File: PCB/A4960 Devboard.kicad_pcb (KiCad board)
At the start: 2 copper layers, 56 parts, among them IC1 ATMEGA8-AI, P1 CONN_02X03, P2 CONN_01X02, P3 CONN_01X03, P4 CONN_01X03, Q1 Q_NMOS_GDS_old, Q2 Q_NMOS_GDS_old, Q3 Q_NMOS_GDS_old, Q4 Q_NMOS_GDS_old, Q5 Q_NMOS_GDS_old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

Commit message: PCB weiter
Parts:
- moved Q6 39.8 mm to (232.2, 85.5)
- moved Q5 39.4 mm to (232.2, 77.5)
- moved U2 30.7 mm to (228.3, 99.8)
- moved U1 27.9 mm to (175.4, 86.7)
- moved Q3 27.3 mm to (223.0, 77.5), turned to 0 degrees
- moved P4 26.4 mm to (221.0, 68.3), turned to 90 degrees
- moved P2 16.4 mm to (206.2, 68.6), turned to 270 degrees
- moved Q4 12.9 mm to (223.0, 85.6), turned to 0 degrees
- moved IC1 12.7 mm to (204.0, 99.8)
- moved C21 5.80 mm to (189.6, 74.7)
- moved Q1 0.25 mm to (213.9, 77.5)
- moved Q2 0.25 mm to (213.9, 85.6)

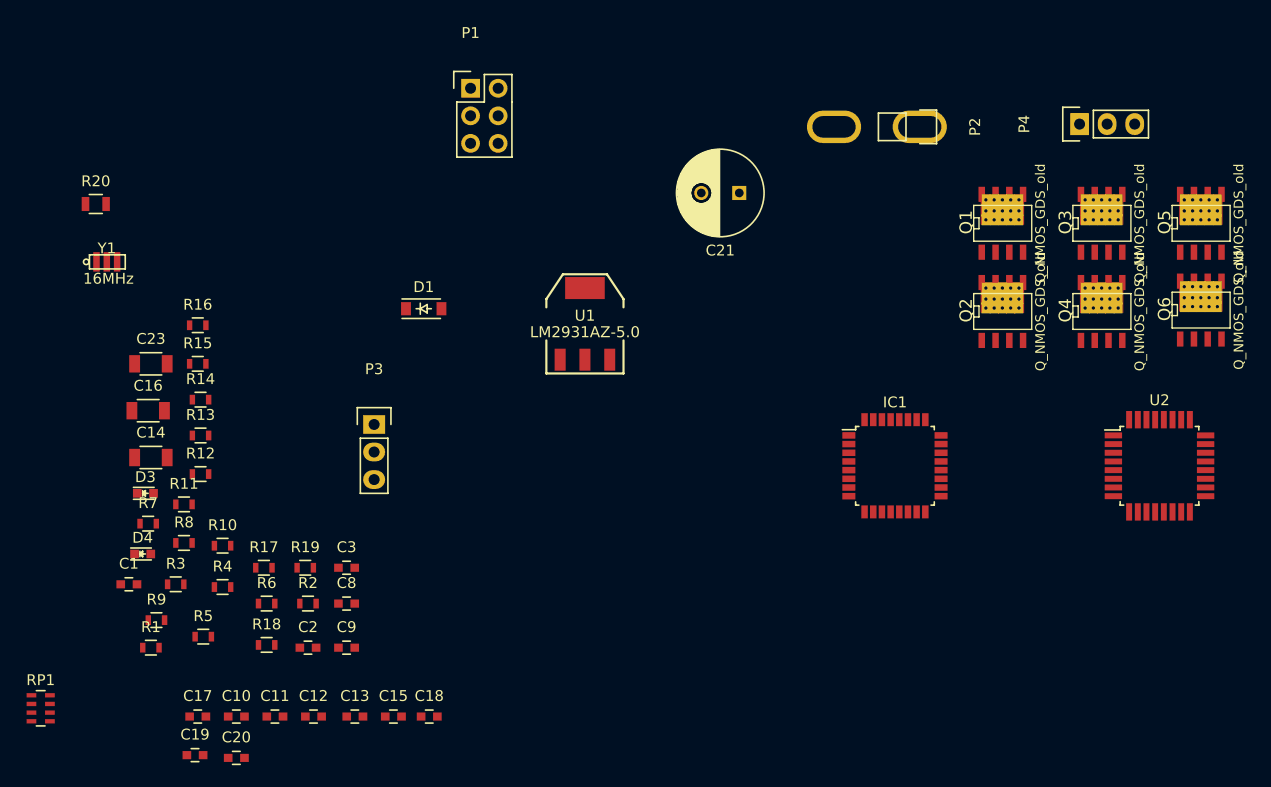
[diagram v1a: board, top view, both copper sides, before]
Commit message: PCB weiter gemcht & neuer Spannungswandler auf 5V
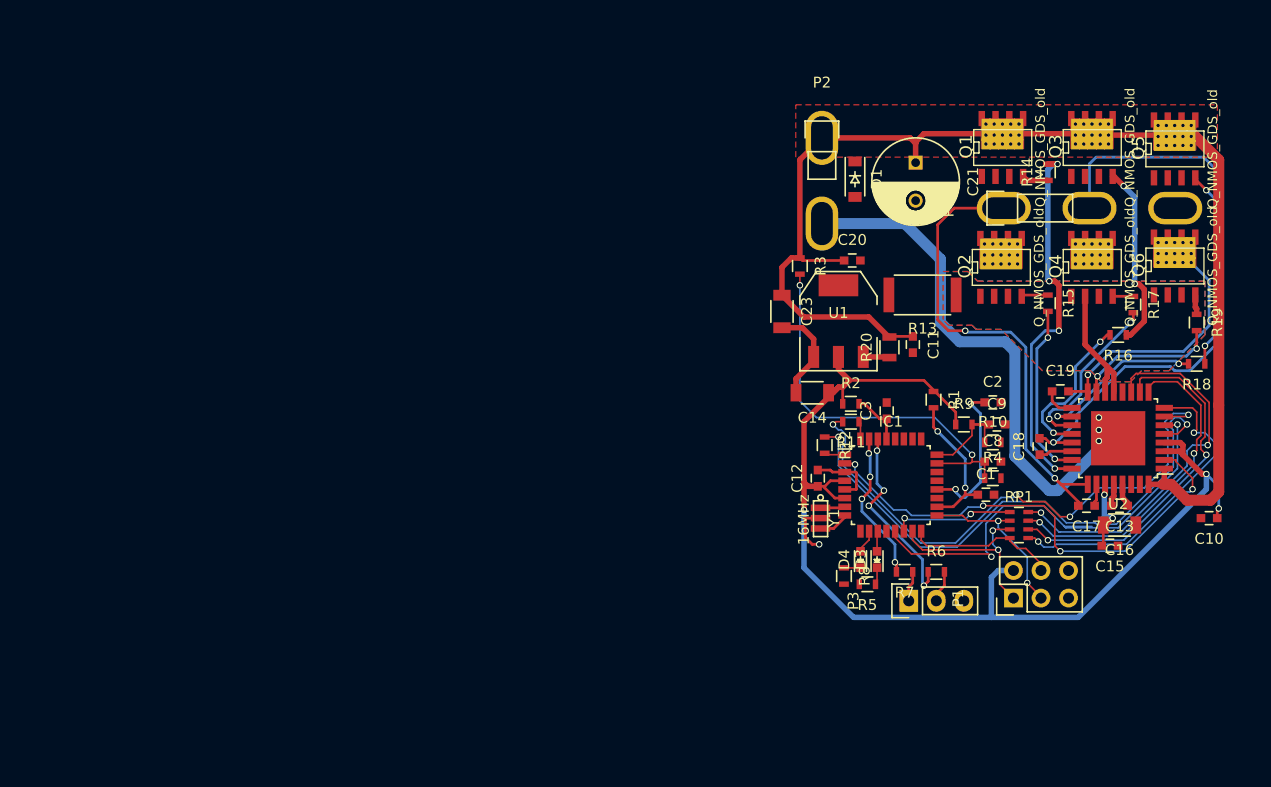
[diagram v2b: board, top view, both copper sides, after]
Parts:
- R13: footprint Resistors_SMD:R_0603 -> Resistors_SMD:R_2512
- U1: value LM2931AZ-5.0 -> LD1117S50TR; footprint toni:SOT223_GND_VO_VI -> TO_SOT_Packages_SMD:SOT-223
- moved RP1 91.7 mm to (215.4, 105.3)
- moved C10 91.5 mm to (232.9, 104.6), turned to 180 degrees
- moved C16 90.2 mm to (224.7, 105.3), turned to 180 degrees
- moved R18 89.6 mm to (231.8, 90.4), turned to 180 degrees
- moved C19 86.5 mm to (219.2, 93.0)
- moved R19 85.2 mm to (231.8, 86.6), turned to 270 degrees
- moved R16 84.8 mm to (224.5, 87.8), turned to 180 degrees
- moved C17 84.2 mm to (221.6, 103.5), turned to 180 degrees
- moved R17 83.7 mm to (225.9, 85.0), turned to 270 degrees
- moved R14 80.9 mm to (218.1, 72.8), turned to 90 degrees
- moved C1 79.4 mm to (212.3, 102.5)
- moved R15 78.6 mm to (218.1, 84.8), turned to 270 degrees
- moved R9 76.6 mm to (210.3, 96.0)
- moved R1 75.7 mm to (207.5, 93.7), turned to 270 degrees
- moved R20 74.3 mm to (203.5, 88.9), turned to 90 degrees
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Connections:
- C10 pad 1: Net-(C10-Pad1) -> +3V3
- U2 pad 3: Net-(C10-Pad1) -> +3V3
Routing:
- net VPP: track 0.00 -> 125.7 mm
- net +3V3: track 0.00 -> 109.8 mm, vias 0 -> 3
- net GND: track 0.00 -> 76.0 mm, vias 0 -> 4
- net /MotorB: track 0.00 -> 55.5 mm, vias 0 -> 1
- net Net-(R11-Pad2): track 0.00 -> 52.0 mm, vias 0 -> 4
- net Net-(R12-Pad1): track 0.00 -> 51.4 mm, vias 0 -> 2
- net Net-(R14-Pad2): track 0.00 -> 47.8 mm, vias 0 -> 4
- net Net-(IC1-Pad2): track 0.00 -> 44.9 mm, vias 0 -> 4
- net /MotorA: track 0.00 -> 44.6 mm, vias 0 -> 2
- net Net-(IC1-Pad13): track 0.00 -> 42.7 mm, vias 0 -> 2
- net /ADC0: track 0.00 -> 36.2 mm, vias 0 -> 2
- net Net-(RP1-Pad8): track 0.00 -> 35.2 mm, vias 0 -> 2
- net Net-(RP1-Pad6): track 0.00 -> 33.6 mm, vias 0 -> 2
- net Net-(Q3-PadG): track 0.00 -> 32.5 mm, vias 0 -> 2
- net Net-(RP1-Pad7): track 0.00 -> 30.7 mm, vias 0 -> 2
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- added copper zone on B.Cu, net /LSS
- added copper zone on F.Cu, net /LSS
- added copper zone on F.Cu, net VPP
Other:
- net class Default: clearance 0.2 -> 0.1778; trace_width 0.25 -> 0.1524
- rule trace_clearance: 0.2 -> 0.1778
- rule trace_min: 0.2 -> 0.1524

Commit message: PCB fertig!
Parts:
- Q1, Q2, Q3, Q4, Q5, Q6: footprint sven:SO8_WITH_Heatpipes -> Sven:SO8_WITH_Heatpipes_New
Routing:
- net GND: track 76.0 -> 121.4 mm, vias 4 -> 11
- net /Reset: track 4.99 -> 34.7 mm, vias 0 -> 4
- net /MotorB: track 55.5 -> 66.0 mm
- net /MotorC: track 23.0 -> 33.0 mm
- net /MotorA: track 44.6 -> 51.8 mm
- net VPP: track 125.7 -> 126.7 mm
- net +3V3: track 109.8 -> 110.6 mm
- net /SCK: track 15.7 -> 15.8 mm, vias 2 -> 1
- added copper zone on F.Cu, net /MotorA
- added copper zone on F.Cu, net /MotorB
- added copper zone on F.Cu, net /MotorC
- added copper zone on B.Cu, net GND
- added copper zone on F.Cu, net GND
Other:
- board outline added: 43.4 x 48.8 mm

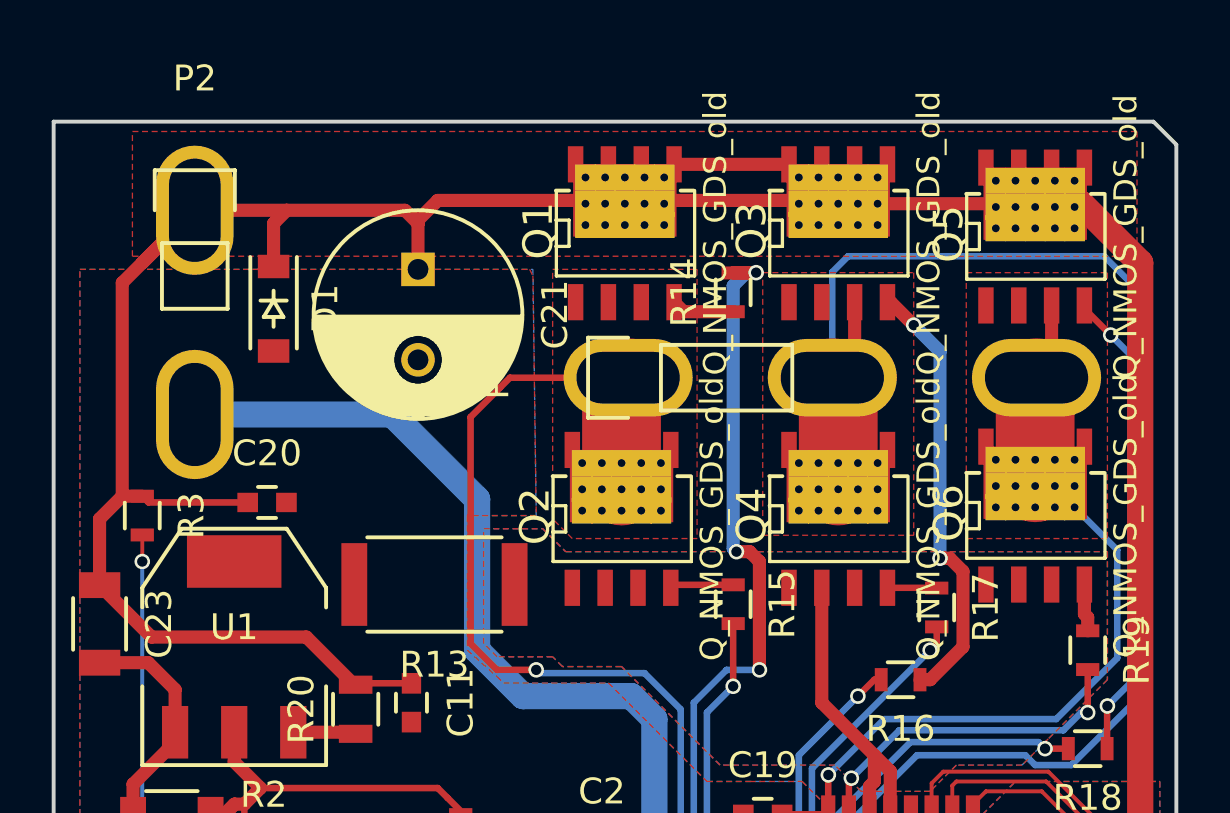
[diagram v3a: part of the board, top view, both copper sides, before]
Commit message: Vcc-Fläche oben eingefügt.
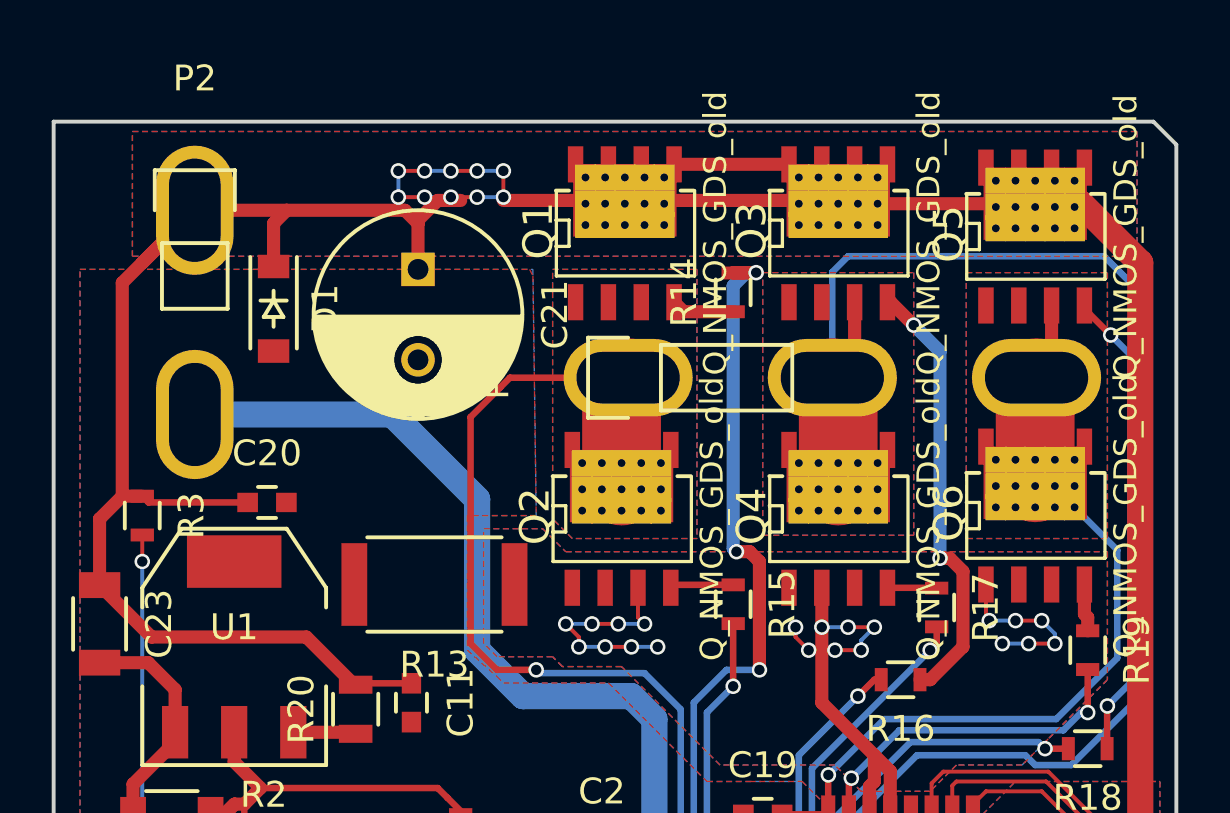
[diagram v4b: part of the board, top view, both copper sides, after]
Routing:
- net /LSS: track 12.4 -> 35.5 mm, vias 0 -> 21
- net VPP: track 126.7 -> 136.0 mm, vias 0 -> 10
- added copper zone on B.Cu, net /MotorA
- added copper zone on B.Cu, net /MotorB
- added copper zone on B.Cu, net /MotorC
- added copper zone on B.Cu, net VPP
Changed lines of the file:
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@@
     (links 256)
     (no_connects 0)
-    (area 0 0 0 0)
+    (area 190.1452 63.3932 235.279001 117.354133)
     (thickness 1.6)
     (drawings 8)
-    (tracks 716)
+    (tracks 790)
     (zones 0)
     (modules 56)
@@
   )
   (setup
-    (last_trace_width 0.508)
+    (last_trace_width 0.1524)
     (user_trace_width 0.1524)
     (user_trace_width 0.254)
@@
   (segment (start 212.229 96.012) (end 212.229 97.663) (width 0.1524) (layer F.Cu) (net 6))
   (segment (start 211.062 96.012) (end 212.229 96.012) (width 0.1524) (layer F.Cu) (net 6))
+  (via (at 209.169 69.088) (size 0.6) (drill 0.4) (layers F.Cu B.Cu) (net 7))
+  (segment (start 207.137 69.088) (end 208.153 69.088) (width 0.1524) (layer F.Cu) (net 7))
+  (via (at 208.153 69.088) (size 0.6) (drill 0.4) (layers F.Cu B.Cu) (net 7))
+  (segment (start 208.153 69.088) (end 209.169 69.088) (width 0.1524) (layer B.Cu) (net 7))
+  (segment (start 209.169 69.215) (end 209.169 69.088) (width 0.1524) (layer F.Cu) (net 7))
+  (segment (start 209.169 69.088) (end 209.169 68.072) (width 0.1524) (layer F.Cu) (net 7))
+  (segment (start 207.518 69.088) (end 207.518 69.215) (width 0.1524) (layer F.Cu) (net 7))
+  (segment (start 207.391 69.215) (end 207.518 69.088) (width 0.1524) (layer F.Cu) (net 7))
+  (segment (start 207.264 69.215) (end 207.391 69.215) (width 0.1524) (layer F.Cu) (net 7))
+  (segment (start 207.137 69.088) (end 207.264 69.215) (width 0.1524) (layer F.Cu) (net 7))
+  (via (at 207.137 69.088) (size 0.6) (drill 0.4) (layers F.Cu B.Cu) (net 7))
+  (segment (start 206.121 69.088) (end 207.137 69.088) (width 0.1524) (layer B.Cu) (net 7))
+  (via (at 206.121 69.088) (size 0.6) (drill 0.4) (layers F.Cu B.Cu) (net 7))
+  (segment (start 205.105 69.088) (end 206.121 69.088) (width 0.1524) (layer F.Cu) (net 7))
+  (via (at 205.105 69.088) (size 0.6) (drill 0.4) (layers F.Cu B.Cu) (net 7))
+  (segment (start 205.105 68.072) (end 205.105 69.088) (width 0.1524) (layer B.Cu) (net 7))
+  (via (at 205.105 68.072) (size 0.6) (drill 0.4) (layers F.Cu B.Cu) (net 7))
+  (segment (start 206.121 68.072) (end 205.105 68.072) (width 0.1524) (layer F.Cu) (net 7))
+  (via (at 206.121 68.072) (size 0.6) (drill 0.4) (layers F.Cu B.Cu) (net 7))
+  (segment (start 207.137 68.072) (end 206.121 68.072) (width 0.1524) (layer B.Cu) (net 7))
+  (via (at 207.137 68.072) (size 0.6) (drill 0.4) (layers F.Cu B.Cu) (net 7))
+  (segment (start 208.153 68.072) (end 207.137 68.072) (width 0.1524) (layer F.Cu) (net 7))
+  (via (at 208.153 68.072) (size 0.6) (drill 0.4) (layers F.Cu B.Cu) (net 7))
+  (segment (start 209.169 68.072) (end 208.153 68.072) (width 0.1524) (layer B.Cu) (net 7))
+  (via (at 209.169 68.072) (size 0.6) (drill 0.4) (layers F.Cu B.Cu) (net 7))
   (segment (start 194.425 80.657) (end 194.425 72.402) (width 0.508) (layer F.Cu) (net 7))
   (segment (start 194.425 72.402) (end 197.231 69.596) (width 0.508) (layer F.Cu) (net 7))
@@
   (segment (start 228.668 101.532) (end 228.786 101.414) (width 0.508) (layer F.Cu) (net 7))
   (segment (start 205.867 70.104) (end 205.867 69.977) (width 0.508) (layer F.Cu) (net 7))
-  (segment (start 206.629 69.215) (end 222.123 69.215) (width 0.508) (layer F.Cu) (net 7))
   (segment (start 205.867 69.977) (end 206.629 69.215) (width 0.508) (layer F.Cu) (net 7))
+  (segment (start 206.629 69.215) (end 207.518 69.215) (width 0.508) (layer F.Cu) (net 7))
+  (segment (start 209.169 69.215) (end 222.123 69.215) (width 0.508) (layer F.Cu) (net 7))
   (segment (start 222.123 69.215) (end 222.25 69.342) (width 0.508) (layer F.Cu) (net 7))
   (segment (start 222.25 69.342) (end 229.743 69.342) (width 0.508) (layer F.Cu) (net 7))
@@
   (segment (start 200.781 97.35) (end 200.781 95.891) (width 0.1524) (layer F.Cu) (net 41))
   (segment (start 200.781 95.891) (end 200.648 95.758) (width 0.1524) (layer F.Cu) (net 41))
+  (segment (start 214.376 84.201) (end 214.376 85.344) (width 0.1524) (layer F.Cu) (net 42) (status 400000))
+  (segment (start 214.376 85.344) (end 214.63 85.598) (width 0.1524) (layer F.Cu) (net 42))
+  (via (at 214.63 85.598) (size 0.6) (drill 0.4) (layers F.Cu B.Cu) (net 42))
+  (segment (start 214.63 85.598) (end 213.614 85.598) (width 0.1524) (layer B.Cu) (net 42))
+  (via (at 213.614 85.598) (size 0.6) (drill 0.4) (layers F.Cu B.Cu) (net 42))
+  (segment (start 213.614 85.598) (end 212.598 85.598) (width 0.1524) (layer F.Cu) (net 42))
+  (via (at 212.598 85.598) (size 0.6) (drill 0.4) (layers F.Cu B.Cu) (net 42))
+  (segment (start 212.598 85.598) (end 211.582 85.598) (width 0.1524) (layer B.Cu) (net 42))
+  (via (at 211.582 85.598) (size 0.6) (drill 0.4) (layers F.Cu B.Cu) (net 42))
+  (segment (start 211.582 85.598) (end 212.09 86.106) (width 0.1524) (layer F.Cu) (net 42))
+  (segment (start 212.09 86.106) (end 212.09 86.487) (width 0.1524) (layer F.Cu) (net 42))
+  (via (at 212.09 86.487) (size 0.6) (drill 0.4) (layers F.Cu B.Cu) (net 42))
+  (segment (start 212.09 86.487) (end 213.106 86.487) (width 0.1524) (layer B.Cu) (net 42))
+  (via (at 213.106 86.487) (size 0.6) (drill 0.4) (layers F.Cu B.Cu) (net 42))
+  (segment (start 213.106 86.487) (end 214.122 86.487) (width 0.1524) (layer F.Cu) (net 42))
+  (via (at 214.122 86.487) (size 0.6) (drill 0.4) (layers F.Cu B.Cu) (net 42))
+  (segment (start 214.122 86.487) (end 215.138 86.487) (width 0.1524) (layer B.Cu) (net 42))
+  (via (at 215.138 86.487) (size 0.6) (drill 0.4) (layers F.Cu B.Cu) (net 42))
+  (segment (start 227.838 84.074) (end 227.838 85.344) (width 0.1524) (layer F.Cu) (net 42) (status 400000))
+  (segment (start 227.838 85.344) (end 227.965 85.471) (width 0.1524) (layer F.Cu) (net 42))
+  (via (at 227.965 85.471) (size 0.6) (drill 0.4) (layers F.Cu B.Cu) (net 42))
+  (segment (start 227.965 85.471) (end 228.981 85.471) (width 0.1524) (layer B.Cu) (net 42))
+  (via (at 228.981 85.471) (size 0.6) (drill 0.4) (layers F.Cu B.Cu) (net 42))
+  (segment (start 228.981 85.471) (end 229.997 85.471) (width 0.1524) (layer F.Cu) (net 42))
+  (via (at 229.997 85.471) (size 0.6) (drill 0.4) (layers F.Cu B.Cu) (net 42))
+  (segment (start 229.997 85.471) (end 230.505 85.979) (width 0.1524) (layer B.Cu) (net 42))
+  (segment (start 230.505 85.979) (end 230.505 86.36) (width 0.1524) (layer B.Cu) (net 42))
+  (via (at 230.505 86.36) (size 0.6) (drill 0.4) (layers F.Cu B.Cu) (net 42))
+  (segment (start 230.505 86.36) (end 229.489 86.36) (width 0.1524) (layer F.Cu) (net 42))
+  (via (at 229.489 86.36) (size 0.6) (drill 0.4) (layers F.Cu B.Cu) (net 42))
+  (segment (start 229.489 86.36) (end 228.473 86.36) (width 0.1524) (layer B.Cu) (net 42))
+  (via (at 228.473 86.36) (size 0.6) (drill 0.4) (layers F.Cu B.Cu) (net 42))
+  (segment (start 221.488 84.201) (end 221.488 85.725) (width 0.1524) (layer F.Cu) (net 42) (status 400000))
+  (via (at 221.488 85.725) (size 0.6) (drill 0.4) (layers F.Cu B.Cu) (net 42))
+  (segment (start 221.488 85.725) (end 222.504 85.725) (width 0.1524) (layer B.Cu) (net 42))
+  (via (at 222.504 85.725) (size 0.6) (drill 0.4) (layers F.Cu B.Cu) (net 42))
+  (segment (start 222.504 85.725) (end 223.52 85.725) (width 0.1524) (layer F.Cu) (net 42))
+  (via (at 223.52 85.725) (size 0.6) (drill 0.4) (layers F.Cu B.Cu) (net 42))
+  (segment (start 223.52 85.725) (end 223.012 86.233) (width 0.1524) (layer B.Cu) (net 42))
+  (segment (start 223.012 86.233) (end 223.012 86.614) (width 0.1524) (layer B.Cu) (net 42))
+  (via (at 223.012 86.614) (size 0.6) (drill 0.4) (layers F.Cu B.Cu) (net 42))
+  (segment (start 223.012 86.614) (end 221.996 86.614) (width 0.1524) (layer F.Cu) (net 42))
+  (via (at 221.996 86.614) (size 0.6) (drill 0.4) (layers F.Cu B.Cu) (net 42))
+  (segment (start 221.996 86.614) (end 220.98 86.614) (width 0.1524) (layer B.Cu) (net 42))
+  (via (at 220.98 86.614) (size 0.6) (drill 0.4) (layers F.Cu B.Cu) (net 42))
+  (segment (start 220.98 86.614) (end 220.472 86.106) (width 0.1524) (layer F.Cu) (net 42))
+  (segment (start 220.472 86.106) (end 220.472 85.725) (width 0.1524) (layer F.Cu) (net 42))
+  (via (at 220.472 85.725) (size 0.6) (drill 0.4) (layers F.Cu B.Cu) (net 42))
   (segment (start 224.136 93.032) (end 224.136 91.294) (width 0.508) (layer F.Cu) (net 42))
   (segment (start 224.136 91.294) (end 223.52 90.678) (width 0.508) (layer F.Cu) (net 42))
@@
     (connect_pads (clearance 0.508))
     (min_thickness 0.254)
+    (fill yes (arc_segments 16) (thermal_gap 0.508) (thermal_bridge_width 0.508))
+    (polygon
+      (pts
+        (xy 227.076 72.009) (xy 232.537 72.009) (xy 232.537 82.296) (xy 227.076 82.296)
+      )
+    )
+  )
+  (zone (net 7) (net_name VPP) (layer B.Cu) (hatch edge 0.508)
+    (connect_pads (clearance 0.508))
+    (min_thickness 0.254)
+    (fill yes (arc_segments 16) (thermal_gap 0.508) (thermal_bridge_width 0.508))
+    (polygon
+      (pts
+        (xy 194.818 66.548) (xy 233.68 66.548) (xy 233.68 71.374) (xy 194.818 71.374)
+      )
+    )
+  )
+  (zone (net 13) (net_name /MotorA) (layer B.Cu) (hatch edge 0.508)
+    (connect_pads (clearance 0.508))
+    (min_thickness 0.254)
+    (fill yes (arc_segments 16) (thermal_gap 0.508) (thermal_bridge_width 0.508))
+    (polygon
+      (pts
+        (xy 211.074 71.882) (xy 216.662 71.882) (xy 216.662 82.296) (xy 211.836 82.296) (xy 211.074 81.534)
+      )
+    )
+  )
+  (zone (net 15) (net_name /MotorB) (layer B.Cu) (hatch edge 0.508)
+    (connect_pads (clearance 0.508))
+    (min_thickness 0.254)
+    (fill yes (arc_segments 16) (thermal_gap 0.508) (thermal_bridge_width 0.508))
+    (polygon
+      (pts
+        (xy 219.202 72.009) (xy 225.044 72.009) (xy 225.044 82.169) (xy 219.202 82.169)
+      )
+    )
+  )
+  (zone (net 17) (net_name /MotorC) (layer B.Cu) (hatch edge 0.508)
+    (connect_pads (clearance 0.508))
+    (min_thickness 0.254)
